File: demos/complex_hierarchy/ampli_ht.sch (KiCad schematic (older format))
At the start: 29 parts, among them P5 CONN_2, P6 CONN_2, Q5 MPAS92, Q6 MPAS42, Q7 MPAS92, Q8 MPAS42, U4 LM358N

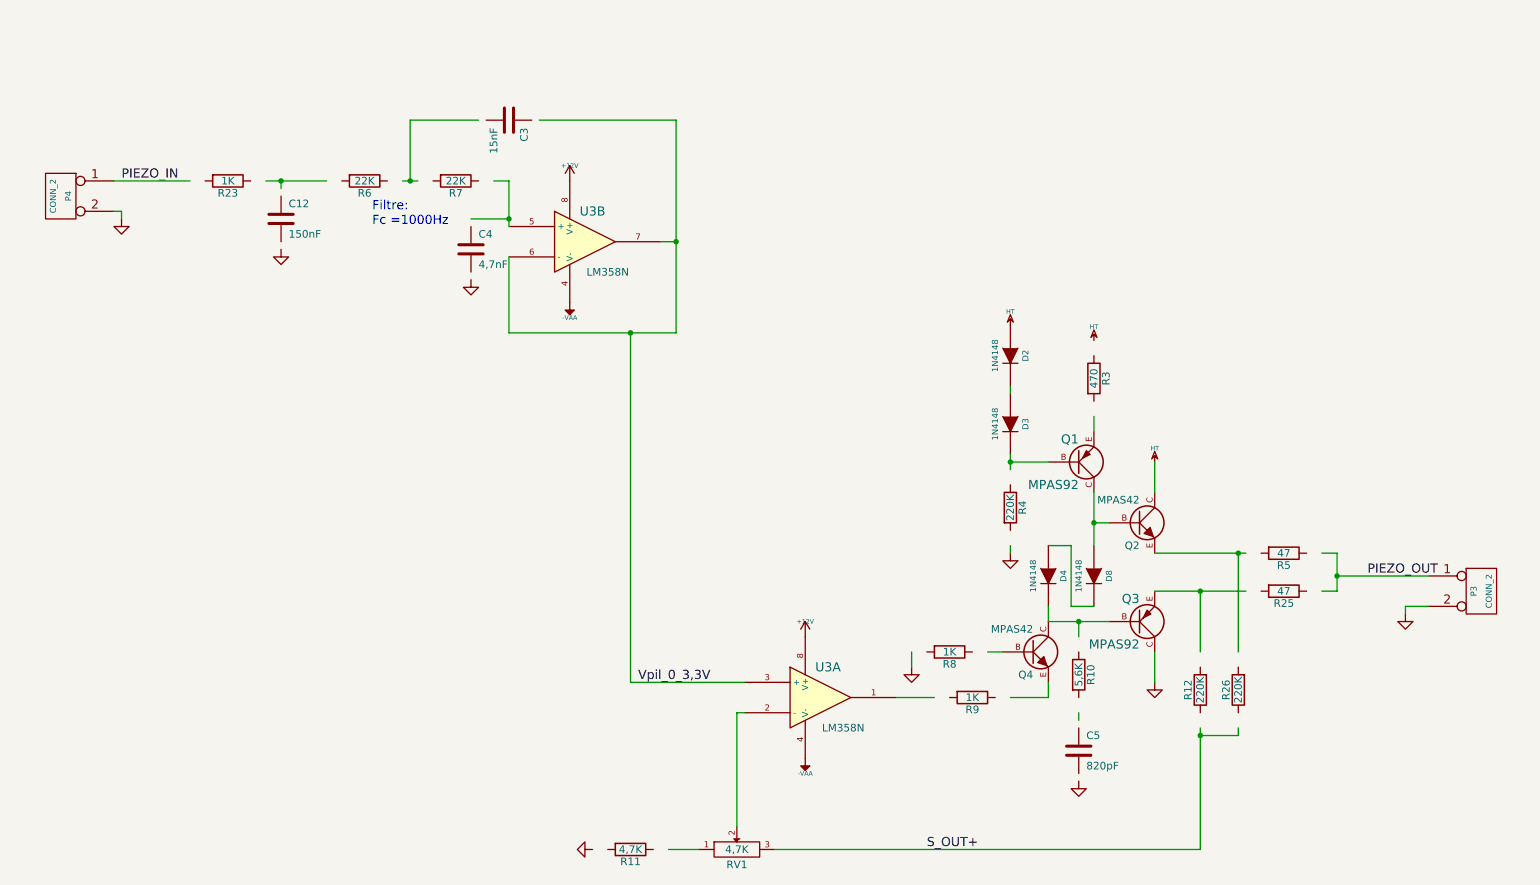
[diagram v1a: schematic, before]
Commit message: Update demo files. A minor code cleaning.
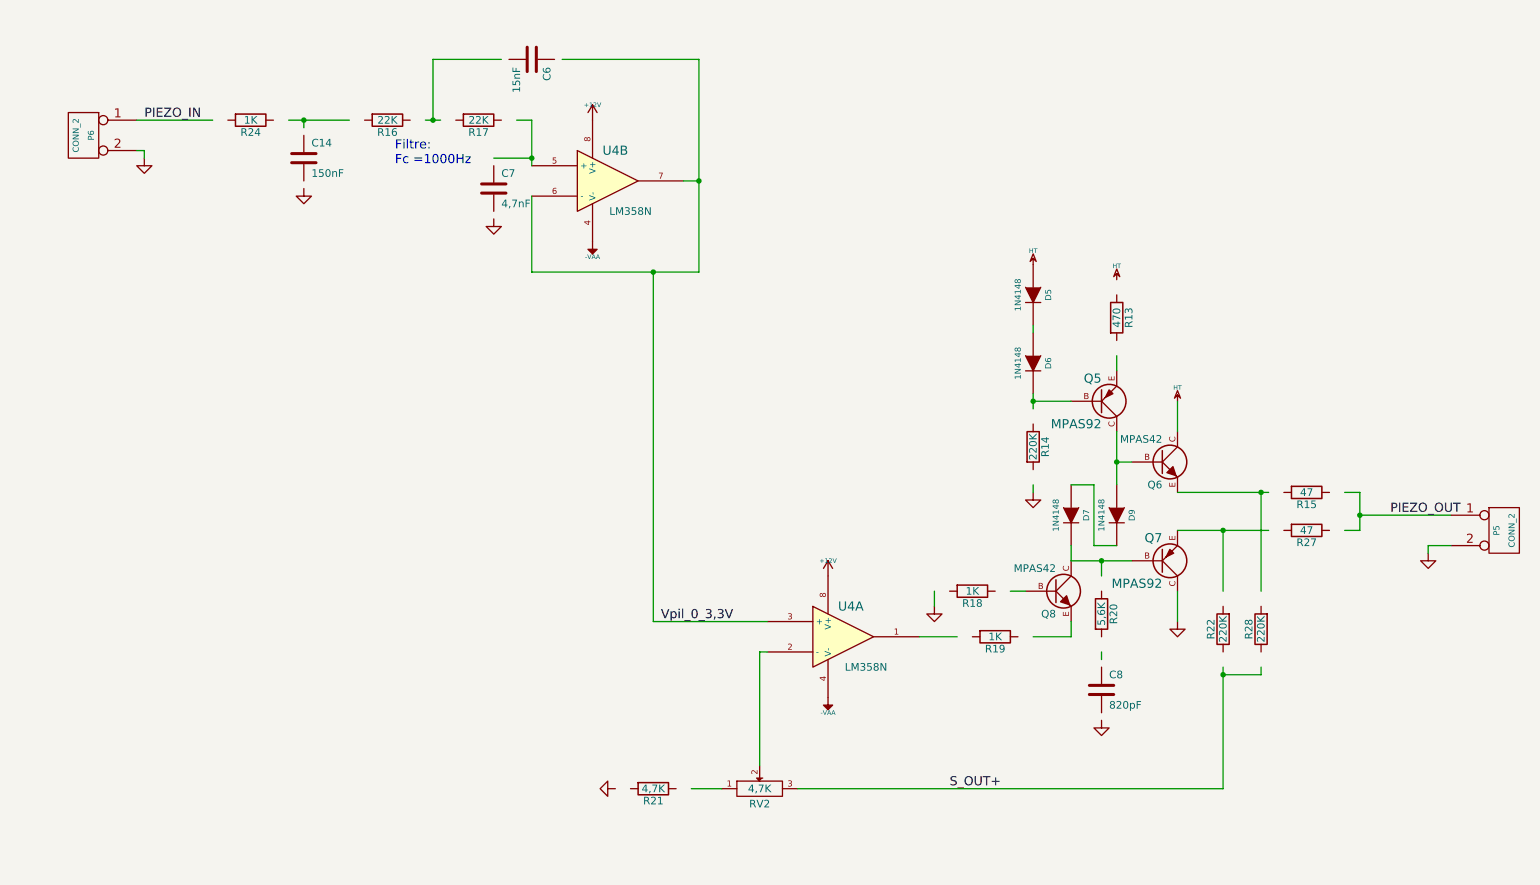
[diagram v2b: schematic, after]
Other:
- moved on the sheet: C14, C6, C7, C8, D5, D6, D7, D9, P5, P6, Q5, Q6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

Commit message: Update demo files
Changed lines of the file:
@@
 LIBS:interface
 LIBS:special
-LIBS:complex_hierarchy-cache
 EELAYER 24 0
 EELAYER END
 $Descr A4 11693 8268
 encoding utf-8
-Sheet 2 3
+Sheet 3 3
 Title ""
 Date "1 apr 2010"
@@
 AR Path="/4B3A1333/4B617B88" Ref="R26"  Part="1"
 AR Path="/4B3A13A4/4B617B88" Ref="R28"  Part="1"
-F 0 "R28" V 9230 5350 50  0000 C CNN
+F 0 "R26" V 9230 5350 50  0000 C CNN
 F 1 "220K" V 9150 5350 50  0000 C CNN
 F 2 "" H 9150 5350 60  0001 C CNN
@@
 AR Path="/4B3A1333/4B616B96" Ref="R25"  Part="1"
 AR Path="/4B3A13A4/4B616B96" Ref="R27"  Part="1"
-F 0 "R27" V 9530 4700 50  0000 C CNN
+F 0 "R25" V 9530 4700 50  0000 C CNN
 F 1 "47" V 9450 4700 50  0000 C CNN
 F 2 "" H 9450 4700 60  0001 C CNN
@@
 AR Path="/4B3A1333/4B616AFA" Ref="D8"  Part="1"
 AR Path="/4B3A13A4/4B616AFA" Ref="D9"  Part="1"
-F 0 "D9" H 8200 4700 40  0000 C CNN
+F 0 "D8" H 8200 4700 40  0000 C CNN
 F 1 "1N4148" H 8200 4500 40  0000 C CNN
 F 2 "" H 8200 4600 60  0001 C CNN
@@
 AR Path="/4B3A1333/4B61688C" Ref="R10"  Part="1"
 AR Path="/4B3A13A4/4B61688C" Ref="R20"  Part="1"
-F 0 "R20" V 8180 5250 50  0000 C CNN
+F 0 "R10" V 8180 5250 50  0000 C CNN
 F 1 "5,6K" V 8100 5250 50  0000 C CNN
 F 2 "" H 8100 5250 60  0001 C CNN
@@
 AR Path="/4B3A1333/4B4F3641" Ref="C12"  Part="1"
 AR Path="/4B3A13A4/4B4F3641" Ref="C14"  Part="1"
-F 0 "C14" H 2900 2350 50  0000 L CNN
+F 0 "C12" H 2900 2350 50  0000 L CNN
 F 1 "150nF" H 2900 2150 50  0000 L CNN
 F 2 "" H 2850 2250 60  0001 C CNN
@@
 AR Path="/4B3A1333/4B4F363E" Ref="R23"  Part="1"
 AR Path="/4B3A13A4/4B4F363E" Ref="R24"  Part="1"
-F 0 "R24" V 2580 2000 50  0000 C CNN
+F 0 "R23" V 2580 2000 50  0000 C CNN
 F 1 "1K" V 2500 2000 50  0000 C CNN
 F 2 "" H 2500 2000 60  0001 C CNN
@@
 AR Path="/4B3A13A4/4B3A137D" Ref="Q6"  Part="1"
 AR Path="/4B3A1333/4B3A137D" Ref="Q2"  Part="1"
-F 0 "Q6" H 8500 4100 50  0000 R CNN
+F 0 "Q2" H 8500 4100 50  0000 R CNN
 F 1 "MPAS42" H 8500 4400 50  0000 R CNN
 F 2 "" H 8500 4250 60  0001 C CNN
@@
 AR Path="/4B3A13A4/4B3A137C" Ref="Q7"  Part="1"
 AR Path="/4B3A1333/4B3A137C" Ref="Q3"  Part="1"
-F 0 "Q7" H 8500 4750 60  0000 R CNN
+F 0 "Q3" H 8500 4750 60  0000 R CNN
 F 1 "MPAS92" H 8500 5050 60  0000 R CNN
 F 2 "" H 8500 4900 60  0001 C CNN
@@
 AR Path="/4B3A13A4/4B3A137B" Ref="D7"  Part="1"
 AR Path="/4B3A1333/4B3A137B" Ref="D4"  Part="1"
-F 0 "D7" H 7900 4700 40  0000 C CNN
+F 0 "D4" H 7900 4700 40  0000 C CNN
 F 1 "1N4148" H 7900 4500 40  0000 C CNN
 F 2 "" H 7900 4600 60  0001 C CNN
@@
 AR Path="/4B3A13A4/4B3A1379" Ref="Q8"  Part="1"
 AR Path="/4B3A1333/4B3A1379" Ref="Q4"  Part="1"
-F 0 "Q8" H 7800 4950 50  0000 R CNN
+F 0 "Q4" H 7800 4950 50  0000 R CNN
 F 1 "MPAS42" H 7800 5250 50  0000 R CNN
 F 2 "" H 7800 5100 60  0001 C CNN
@@
 AR Path="/4B3A13A4/4B3A1377" Ref="D6"  Part="1"
 AR Path="/4B3A1333/4B3A1377" Ref="D3"  Part="1"
-F 0 "D6" H 7650 3700 40  0000 C CNN
+F 0 "D3" H 7650 3700 40  0000 C CNN
 F 1 "1N4148" H 7650 3500 40  0000 C CNN
 F 2 "" H 7650 3600 60  0001 C CNN
@@
 AR Path="/4B3A13A4/4B3A1376" Ref="R13"  Part="1"
 AR Path="/4B3A1333/4B3A1376" Ref="R3"  Part="1"
-F 0 "R13" V 8280 3300 50  0000 C CNN
+F 0 "R3" V 8280 3300 50  0000 C CNN
 F 1 "470" V 8200 3300 50  0000 C CNN
 F 2 "" H 8200 3300 60  0001 C CNN
@@
 AR Path="/4B3A13A4/4B3A1375" Ref="D5"  Part="1"
 AR Path="/4B3A1333/4B3A1375" Ref="D2"  Part="1"
-F 0 "D5" H 7650 3250 40  0000 C CNN
+F 0 "D2" H 7650 3250 40  0000 C CNN
 F 1 "1N4148" H 7650 3050 40  0000 C CNN
 F 2 "" H 7650 3150 60  0001 C CNN
@@
 AR Path="/4B3A13A4/4B3A1374" Ref="R14"  Part="1"
 AR Path="/4B3A1333/4B3A1374" Ref="R4"  Part="1"
-F 0 "R14" V 7730 4150 50  0000 C CNN
+F 0 "R4" V 7730 4150 50  0000 C CNN
 F 1 "220K" V 7650 4150 50  0000 C CNN
 F 2 "" H 7650 4150 60  0001 C CNN
@@
 AR Path="/4B3A13A4/4B3A1371" Ref="R18"  Part="1"
 AR Path="/4B3A1333/4B3A1371" Ref="R8"  Part="1"
-F 0 "R18" V 7330 5100 50  0000 C CNN
+F 0 "R8" V 7330 5100 50  0000 C CNN
 F 1 "1K" V 7250 5100 50  0000 C CNN
 F 2 "" H 7250 5100 60  0001 C CNN
@@
 AR Path="/4B3A13A4/4B3A1370" Ref="R22"  Part="1"
 AR Path="/4B3A1333/4B3A1370" Ref="R12"  Part="1"
-F 0 "R22" V 8980 5350 50  0000 C CNN
+F 0 "R12" V 8980 5350 50  0000 C CNN
 F 1 "220K" V 8900 5350 50  0000 C CNN
 F 2 "" H 8900 5350 60  0001 C CNN
@@
 AR Path="/4B3A13A4/4B3A136D" Ref="R19"  Part="1"
 AR Path="/4B3A1333/4B3A136D" Ref="R9"  Part="1"
-F 0 "R19" V 7480 5400 50  0000 C CNN
+F 0 "R9" V 7480 5400 50  0000 C CNN
 F 1 "1K" V 7400 5400 50  0000 C CNN
 F 2 "" H 7400 5400 60  0001 C CNN
@@
 AR Path="/4B3A13A4/4B3A136C" Ref="P5"  Part="1"
 AR Path="/4B3A1333/4B3A136C" Ref="P3"  Part="1"
-F 0 "P5" V 10700 4700 40  0000 C CNN
+F 0 "P3" V 10700 4700 40  0000 C CNN
 F 1 "CONN_2" V 10800 4700 40  0000 C CNN
 F 2 "" H 10750 4700 60  0001 C CNN
@@
 AR Path="/4B3A13A4/4B3A136B" Ref="R16"  Part="1"
 AR Path="/4B3A1333/4B3A136B" Ref="R6"  Part="1"
-F 0 "R16" V 3480 2000 50  0000 C CNN
+F 0 "R6" V 3480 2000 50  0000 C CNN
 F 1 "22K" V 3400 2000 50  0000 C CNN
 F 2 "" H 3400 2000 60  0001 C CNN
@@
 AR Path="/4B3A13A4/4B3A1368" Ref="U4"  Part="1"
 AR Path="/4B3A1333/4B3A1368" Ref="U3"  Part="1"
-F 0 "U4" H 6450 5600 60  0000 C CNN
+F 0 "U3" H 6450 5600 60  0000 C CNN
 F 1 "LM358N" H 6550 5200 50  0000 C CNN
 F 2 "" H 6400 5400 60  0001 C CNN
@@
 AR Path="/4B3A13A4/4B3A1367" Ref="P6"  Part="1"
 AR Path="/4B3A1333/4B3A1367" Ref="P4"  Part="1"
-F 0 "P6" V 1350 2100 40  0000 C CNN
+F 0 "P4" V 1350 2100 40  0000 C CNN
 F 1 "CONN_2" V 1450 2100 40  0000 C CNN
 F 2 "" H 1400 2100 60  0001 C CNN
@@
 AR Path="/4B3A13A4/4B3A1366" Ref="C7"  Part="1"
 AR Path="/4B3A1333/4B3A1366" Ref="C4"  Part="1"
-F 0 "C7" H 4150 2550 50  0000 L CNN
+F 0 "C4" H 4150 2550 50  0000 L CNN
 F 1 "4,7nF" H 4150 2350 50  0000 L CNN
 F 2 "" H 4100 2450 60  0001 C CNN
@@
 AR Path="/4B3A13A4/4B3A1365" Ref="C8"  Part="1"
 AR Path="/4B3A1333/4B3A1365" Ref="C5"  Part="1"
-F 0 "C8" H 8150 5850 50  0000 L CNN
+F 0 "C5" H 8150 5850 50  0000 L CNN
 F 1 "820pF" H 8150 5650 50  0000 L CNN
 F 2 "" H 8100 5750 60  0001 C CNN
@@
 AR Path="/4B3A13A4/4B3A1364" Ref="R15"  Part="1"
 AR Path="/4B3A1333/4B3A1364" Ref="R5"  Part="1"
-F 0 "R15" V 9530 4450 50  0000 C CNN
+F 0 "R5" V 9530 4450 50  0000 C CNN
 F 1 "47" V 9450 4450 50  0000 C CNN
 F 2 "" H 9450 4450 60  0001 C CNN
@@
 AR Path="/4B3A13A4/4B3A1362" Ref="R21"  Part="1"
 AR Path="/4B3A1333/4B3A1362" Ref="R11"  Part="1"
-F 0 "R21" V 5230 6400 50  0000 C CNN
+F 0 "R11" V 5230 6400 50  0000 C CNN
 F 1 "4,7K" V 5150 6400 50  0000 C CNN
 F 2 "" H 5150 6400 60  0001 C CNN
@@
 AR Path="/4B3A13A4/4B3A1360" Ref="Q5"  Part="1"
 AR Path="/4B3A1333/4B3A1360" Ref="Q1"  Part="1"
-F 0 "Q5" H 8100 3700 60  0000 R CNN
+F 0 "Q1" H 8100 3700 60  0000 R CNN
 F 1 "MPAS92" H 8100 4000 60  0000 R CNN
 F 2 "" H 8100 3850 60  0001 C CNN
@@
 AR Path="/4B3A13A4/4B3A135C" Ref="U4"  Part="2"
 AR Path="/4B3A1333/4B3A135C" Ref="U3"  Part="2"
-F 0 "U4" H 4900 2600 60  0000 C CNN
+F 0 "U3" H 4900 2600 60  0000 C CNN
 F 1 "LM358N" H 5000 2200 50  0000 C CNN
 F 2 "" H 4850 2400 60  0001 C CNN
@@
 AR Path="/4B3A13A4/4B3A1359" Ref="R17"  Part="1"
 AR Path="/4B3A1333/4B3A1359" Ref="R7"  Part="1"
-F 0 "R17" V 4080 2000 50  0000 C CNN
+F 0 "R7" V 4080 2000 50  0000 C CNN
 F 1 "22K" V 4000 2000 50  0000 C CNN
 F 2 "" H 4000 2000 60  0001 C CNN
@@
 AR Path="/4B3A13A4/4B3A1358" Ref="C6"  Part="1"
 AR Path="/4B3A1333/4B3A1358" Ref="C3"  Part="1"
-F 0 "C6" H 4400 1700 50  0000 L CNN
+F 0 "C3" H 4400 1700 50  0000 L CNN
 F 1 "15nF" H 4400 1500 50  0000 L CNN
 F 2 "" H 4350 1600 60  0001 C CNN
@@
 AR Path="/4B3A13A4/4B3A1357" Ref="RV2"  Part="1"
 AR Path="/4B3A1333/4B3A1357" Ref="RV1"  Part="1"
-F 0 "RV2" H 5850 6300 50  0000 C CNN
+F 0 "RV1" H 5850 6300 50  0000 C CNN
 F 1 "4,7K" H 5850 6400 50  0000 C CNN
 F 2 "" H 5850 6400 60  0001 C CNN

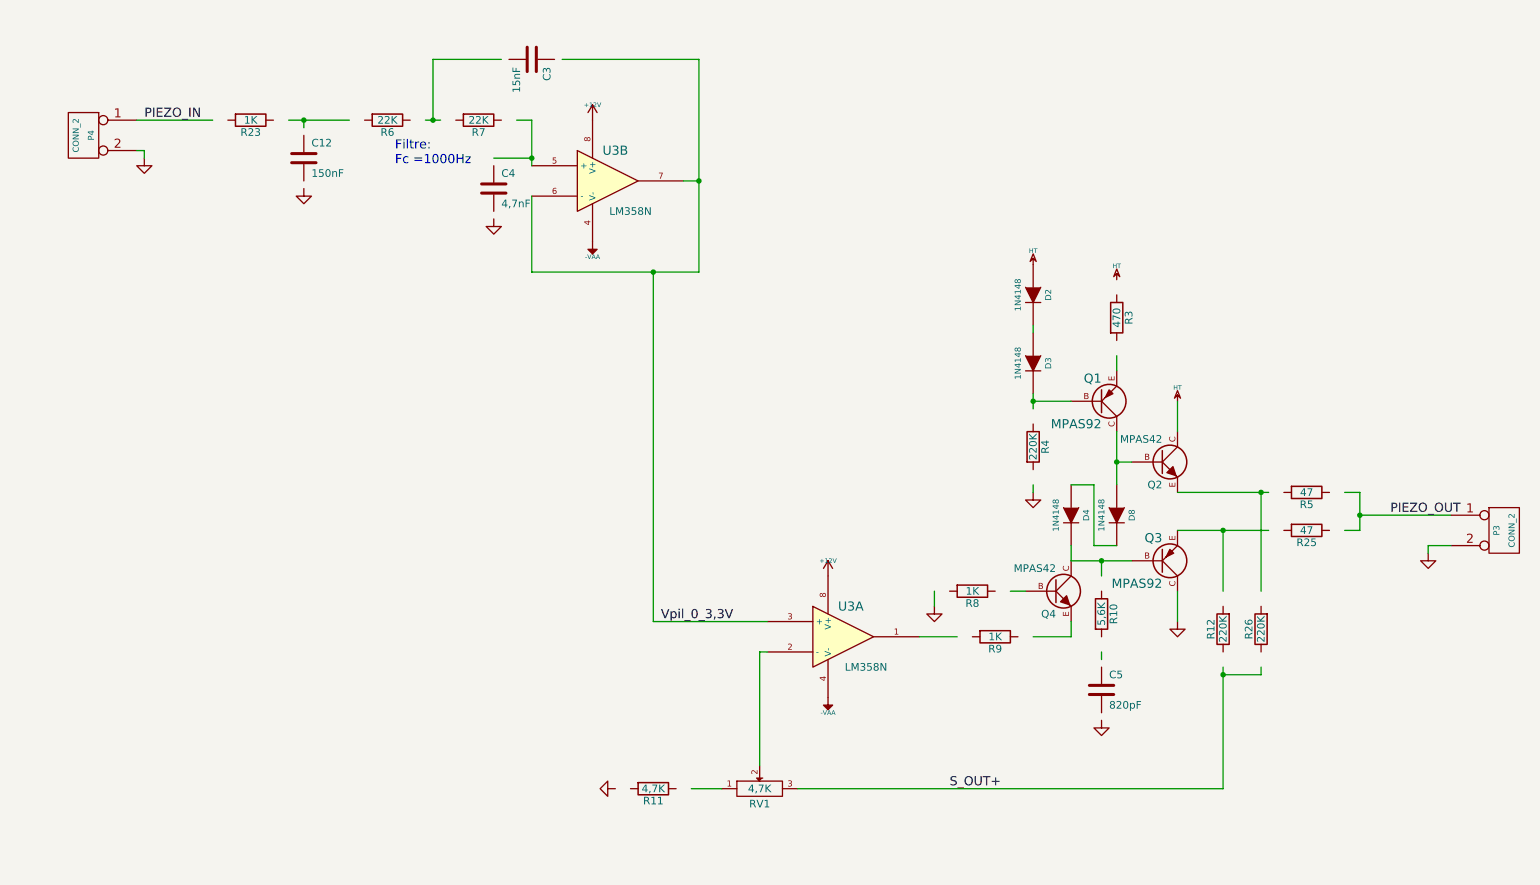
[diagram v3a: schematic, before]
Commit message: demos/ schematic tidying
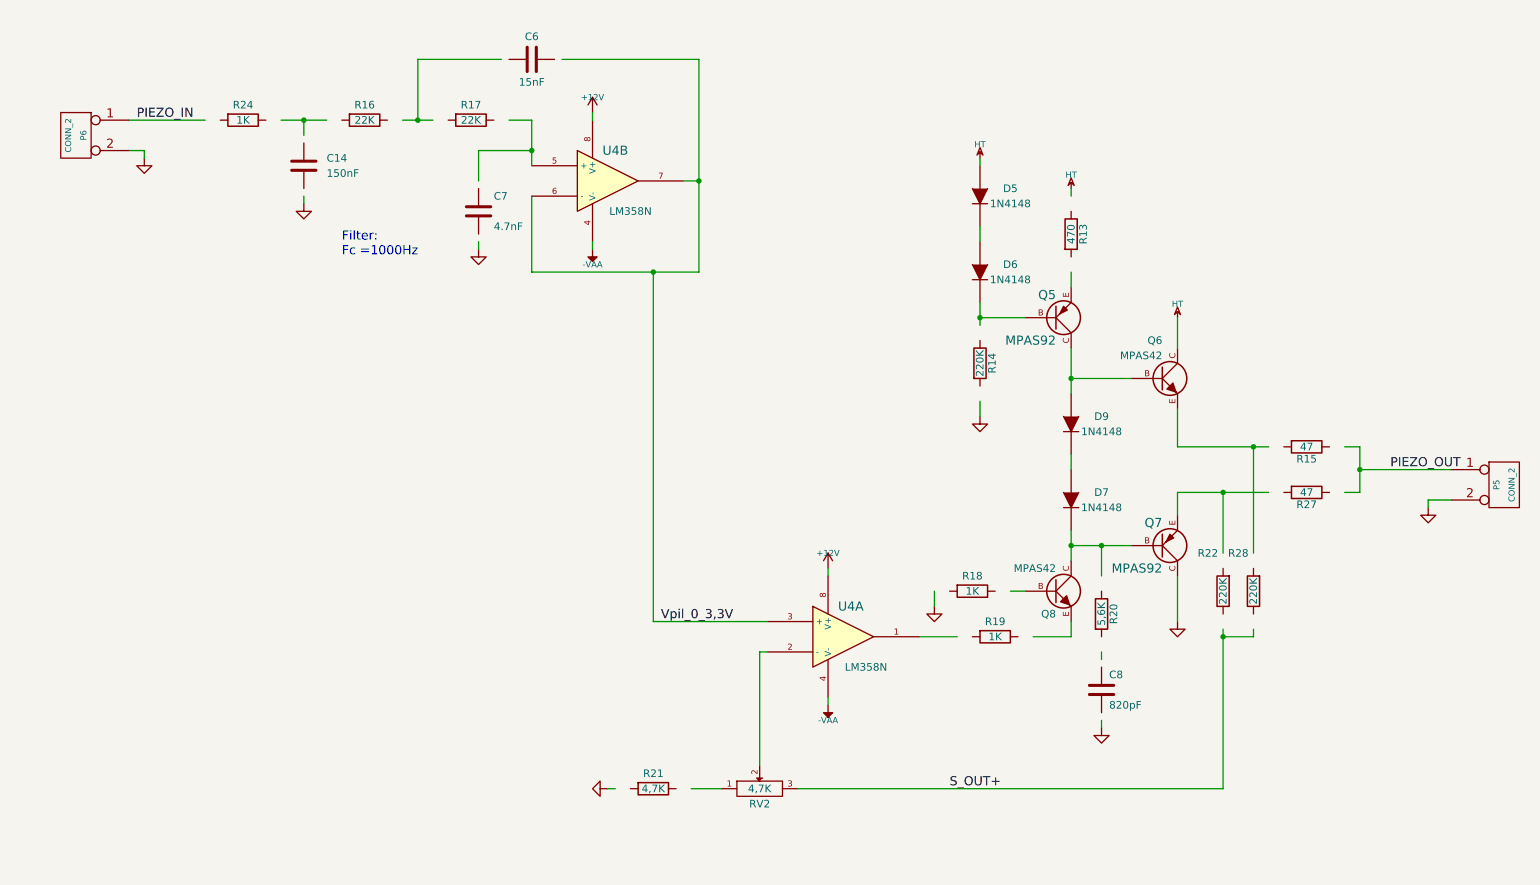
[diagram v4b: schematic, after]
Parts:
- C7: value 4,7nF -> 4.7nF
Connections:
- wire segments 56 -> 80
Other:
- note added: "Filter:\nFc =1000Hz"
- note removed: "Filtre:\nFc =1000Hz"
- moved on the sheet: C14, C7, D5, D6, D7, D9, P5, P6, Q5, Q6, Q7, R13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
